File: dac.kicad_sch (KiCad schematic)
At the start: 30 parts, among them J2 Conn_02x03_Odd_Even, U6 PCM5242RHBR, X1 22.5792Mhz, X2 24.576Mhz

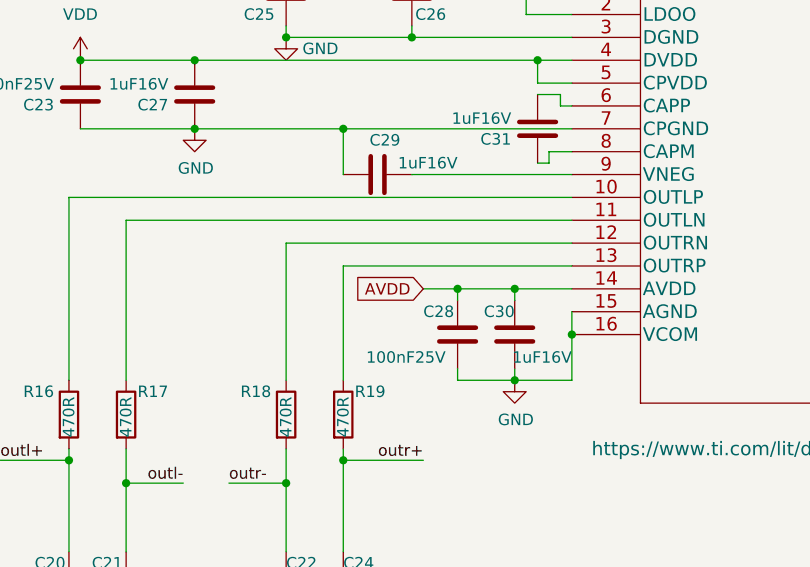
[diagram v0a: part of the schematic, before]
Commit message: Use Power Symbols for analog power
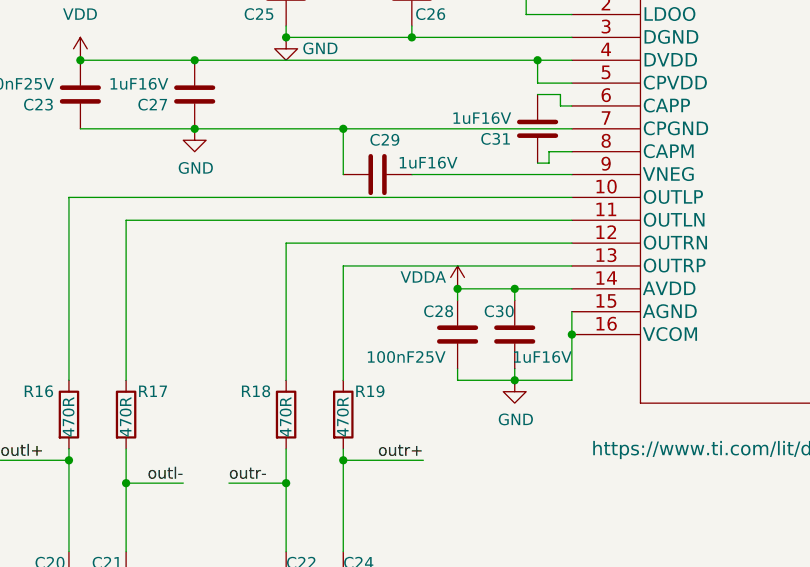
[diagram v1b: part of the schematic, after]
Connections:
- net AVDD renamed VDDA
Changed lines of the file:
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@@
     (comment 2 "License: CERN Open Hardware Licence Version 2 - Permissive")
   )
+  (junction (at 90.17 118.11) (diameter 0) (color 0 0 0 0)
+  )
   (junction (at 199.39 115.57) (diameter 0) (color 0 0 0 0)
   )
@@
   )
   (junction (at 154.94 87.63) (diameter 0) (color 0 0 0 0)
-  )
-  (junction (at 90.17 118.11) (diameter 0) (color 0 0 0 0)
   )
   (junction (at 71.12 90.17) (diameter 0) (color 0 0 0 0)
@@
   )
   (wire (pts (xy 71.12 90.17) (xy 85.09 90.17))
-    (stroke (width 0) (type default))
-  )
-  (wire (pts (xy 90.17 118.11) (xy 86.36 118.11))
     (stroke (width 0) (type default))
   )
@@
     (property "Intersheetrefs" "${INTERSHEET_REFS}" (at 179.1633 90.17 0)
       (effects (font (size 1.27 1.27)) (justify left) hide)
-    )
-  )
-  (global_label "AVDD" (shape input) (at 86.36 118.11 180)
-    (effects (font (size 1.27 1.27)) (justify right))
-    (property "Intersheetrefs" "${INTERSHEET_REFS}" (at 86.36 118.11 0)
-      (effects (font (size 1.27 1.27)) hide)
     )
   )
@@
         )
       )
+    )
+  )
+  (symbol (lib_id "power:VDDA") (at 90.17 118.11 0) (unit 1)
+    (in_bom yes) (on_board yes) (dnp no)
+    (property "Reference" "#PWR038" (at 90.17 121.92 0)
+      (effects (font (size 1.27 1.27)) hide)
+    )
+    (property "Value" "VDDA" (at 86.36 116.84 0)
+      (effects (font (size 1.27 1.27)))
+    )
+    (property "Footprint" "" (at 90.17 118.11 0)
+      (effects (font (size 1.27 1.27)) hide)
+    )
+    (property "Datasheet" "" (at 90.17 118.11 0)
+      (effects (font (size 1.27 1.27)) hide)
+    )
+    (pin "1")
+    (instances
+      (project "pedalboard-soundcard"
+        (path "/257597c6-fbef-4478-b0f4-968f2d6f1866/c0100554-f979-4e8d-b08c-e48cc1e12bdc"
+          (reference "#PWR038") (unit 1)
+        )
+      )

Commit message: Revert to standard RPI headers
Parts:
- J2: footprint Connector_PinHeader_2.54mm:PinHeader_2x03_P2.54mm_Vertical -> pedalboard-soundcard:PinSocket_2x03_P2.54mm_Vertical
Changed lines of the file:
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@@
       (effects (font (size 1.27 1.27)))
     )
-    (property "Footprint" "Connector_PinHeader_2.54mm:PinHeader_2x03_P2.54mm_Vertical" (at 130.81 158.75 0)
+    (property "Footprint" "pedalboard-soundcard:PinSocket_2x03_P2.54mm_Vertical" (at 130.81 158.75 0)
       (effects (font (size 1.27 1.27)) hide)
     )

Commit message: Fix library
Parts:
- U6: symbol zynthiandac-rescue:PCM5242RHBR-pcm5242 -> pedalboard-soundcard:PCM5242RHBR-pcm5242
- X1, X2: symbol zynthiandac-rescue:ASCO-Oscillator -> pedalboard-soundcard:ASCO-Oscillator
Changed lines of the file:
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@@
     )
   )
-  (symbol (lib_id "zynthiandac-rescue:ASCO-Oscillator") (at 214.63 115.57 0) (unit 1)
+  (symbol (lib_id "pedalboard-soundcard:ASCO-Oscillator") (at 214.63 115.57 0) (unit 1)
     (in_bom yes) (on_board yes) (dnp no)
     (property "Reference" "X2" (at 219.71 121.92 0)
@@
     )
   )
-  (symbol (lib_id "zynthiandac-rescue:PCM5242RHBR-pcm5242") (at 102.87 85.09 0) (unit 1)
+  (symbol (lib_id "pedalboard-soundcard:PCM5242RHBR-pcm5242") (at 102.87 85.09 0) (unit 1)
     (in_bom yes) (on_board yes) (dnp no)
     (property "Reference" "U6" (at 125.73 75.2602 0)
@@
     )
   )
-  (symbol (lib_id "zynthiandac-rescue:ASCO-Oscillator") (at 214.63 81.28 0) (unit 1)
+  (symbol (lib_id "pedalboard-soundcard:ASCO-Oscillator") (at 214.63 81.28 0) (unit 1)
     (in_bom yes) (on_board yes) (dnp no)
     (property "Reference" "X1" (at 219.71 87.63 0)
       (effects (font (size 1.27 1.27)) (justify left))
     )
-    (property "Value" "22.5792Mhz" (at 222.25 85.09 0)
-      (effects (font (size 1.27 1.27)) (justify left))
-    )
+    (property "Value" "22.5792Mhz" (at 223.52 85.09 0)
+      (effects (font (size 1.27 1.27)) (justify left))
+    )

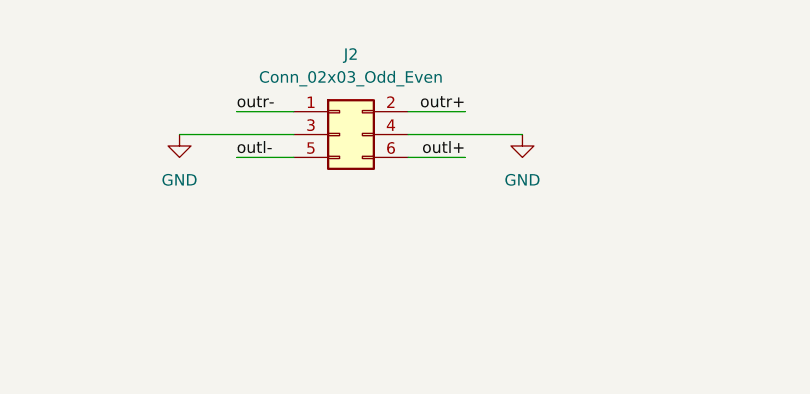
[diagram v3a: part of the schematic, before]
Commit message: Add 3.5mm jack connectors
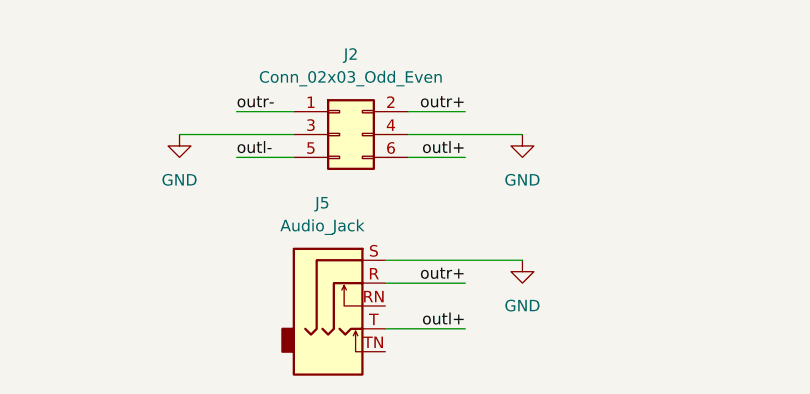
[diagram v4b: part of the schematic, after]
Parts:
- added J5: Audio_Jack, Connector_Audio:Jack_3.5mm_CUI_SJ1-3525N_Horizontal, symbol Connector_Audio:AudioJack3_SwitchTR
- J2: Supplier (none) -> https://www.digikey.ch/de/products/detail/te-connectivity-a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
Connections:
- net GND: now also J5.S
- net outl+: now also J5.T
- net outr+: now also J5.R
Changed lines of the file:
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@@
+    (stroke (width 0) (type default))
+  )
+  (wire (pts (xy 135.89 172.72) (xy 151.13 172.72))
     (stroke (width 0) (type default))
   )
@@
     (stroke (width 0) (type default))
   )
+  (wire (pts (xy 135.89 175.26) (xy 144.78 175.26))
+    (stroke (width 0) (type default))
+  )
   (wire (pts (xy 77.47 135.89) (xy 77.47 137.16))
     (stroke (width 0) (type default))
@@
     (stroke (width 0) (type default))
   )
+  (wire (pts (xy 135.89 180.34) (xy 144.78 180.34))
+    (stroke (width 0) (type default))
+  )
   (wire (pts (xy 238.76 85.09) (xy 238.76 88.9))
     (stroke (width 0) (type default))
@@
     (stroke (width 0) (type default))
   )
+  (label "outl+" (at 144.78 180.34 180) (fields_autoplaced)
+    (effects (font (size 1.27 1.27)) (justify right bottom))
+  )
   (label "outl-" (at 59.69 139.7 180) (fields_autoplaced)
+    (effects (font (size 1.27 1.27)) (justify right bottom))
+  )
+  (label "outr+" (at 144.78 175.26 180) (fields_autoplaced)
     (effects (font (size 1.27 1.27)) (justify right bottom))
   )
@@
     )
   )
+  (symbol (lib_id "Connector_Audio:AudioJack3_SwitchTR") (at 130.81 175.26 0) (unit 1)
+    (in_bom yes) (on_board yes) (dnp no) (fields_autoplaced)
+    (property "Reference" "J5" (at 128.905 166.37 0)
+      (effects (font (size 1.27 1.27)))
+    )
+    (property "Value" "Audio_Jack" (at 128.905 168.91 0)
+      (effects (font (size 1.27 1.27)))
+    )
+    (property "Footprint" "Connector_Audio:Jack_3.5mm_CUI_SJ1-3525N_Horizontal" (at 130.81 175.26 0)
+      (effects (font (size 1.27 1.27)) hide)
+    )
+    (property "Datasheet" "https://www.cuidevices.com/product/resource/sj1-352xng.pdf" (at 130.81 175.26 0)
+      (effects (font (size 1.27 1.27)) hide)
+    )
+    (property "Supplier" "https://www.digikey.ch/de/products/detail/schurter-inc/4833-2320/2644235" (at 130.81 175.26 0)
+      (effects (font (size 1.27 1.27)) hide)
+    )
+    (pin "RN")
+    (pin "S")
+    (pin "R")
+    (pin "TN")
+    (pin "T")
+    (instances
+      (project "pedalboard-soundcard"
+        (path "/257597c6-fbef-4478-b0f4-968f2d6f1866/c0100554-f979-4e8d-b08c-e48cc1e12bdc"
+          (reference "J5") (unit 1)
+        )
+      )
+    )
+  )
   (symbol (lib_id "power:GND") (at 199.39 91.44 0) (unit 1)
     (in_bom yes) (on_board yes) (dnp no)
@@
         (path "/684ba6b6-4674-4c20-b126-c7deb678f8f5"
           (reference "R27") (unit 1)
+        )
+      )
+    )
+  )
+  (symbol (lib_id "power:GND") (at 151.13 172.72 0) (unit 1)
+    (in_bom yes) (on_board yes) (dnp no) (fields_autoplaced)
+    (property "Reference" "#PWR041" (at 151.13 179.07 0)
+      (effects (font (size 1.27 1.27)) hide)
+    )
+    (property "Value" "GND" (at 151.13 177.8 0)
+      (effects (font (size 1.27 1.27)))
+    )
+    (property "Footprint" "" (at 151.13 172.72 0)
+      (effects (font (size 1.27 1.27)) hide)
+    )
+    (property "Datasheet" "" (at 151.13 172.72 0)
+      (effects (font (size 1.27 1.27)) hide)
+    )
+    (pin "1")
+    (instances
+      (project "pedalboard-soundcard"
+        (path "/257597c6-fbef-4478-b0f4-968f2d6f1866/c0100554-f979-4e8d-b08c-e48cc1e12bdc"
+          (reference "#PWR041") (unit 1)
         )
       )
@@
       (effects (font (size 1.27 1.27)) hide)
     )
-    (property "Datasheet" "~" (at 130.81 158.75 0)
-      (effects (font (size 1.27 1.27)) hide)
-    )
-    (property "Supplier" "" (at 130.81 158.75 0)
-      (effects (font (size 1.27 1.27)) hide)
-    )
+    (property "Datasheet" "https://www.te.com/commerce/DocumentDelivery/DDEController?Action=srchrtrv&DocNm=534206&DocType=Customer+Drawing&DocLang=English" (at 130.81 158.75 0)
+      (effects (font (size 1.27 1.27)) hide)
+    )
+    (property "Supplier" "https://www.digikey.ch/de/products/detail/te-connectivity-amp-connectors/5-534206-3/1093005" (at 130.81 158.75 0)
+      (effects (font (size 1.27 1.27)) hide)
+    )

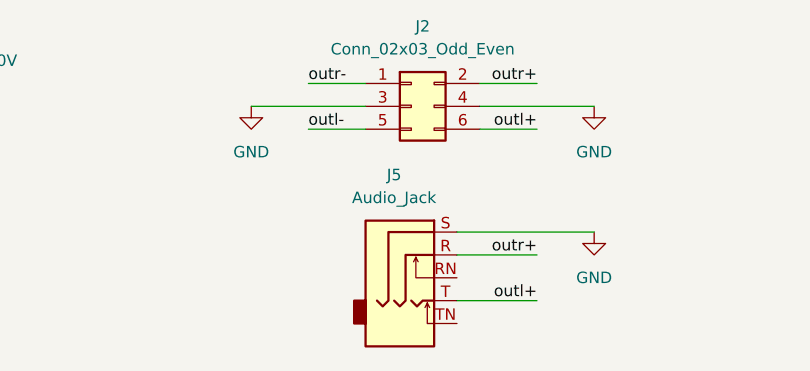
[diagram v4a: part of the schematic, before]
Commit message: DNP 3.5mm jack connectors
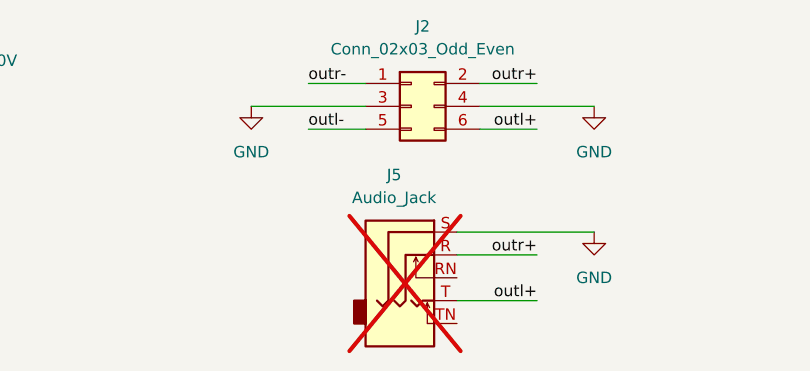
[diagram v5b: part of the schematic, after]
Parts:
- J5: now not fitted
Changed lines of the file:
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@@
   )
   (symbol (lib_id "Connector_Audio:AudioJack3_SwitchTR") (at 130.81 175.26 0) (unit 1)
-    (in_bom yes) (on_board yes) (dnp no) (fields_autoplaced)
+    (in_bom yes) (on_board yes) (dnp yes) (fields_autoplaced)
     (property "Reference" "J5" (at 128.905 166.37 0)
       (effects (font (size 1.27 1.27)))

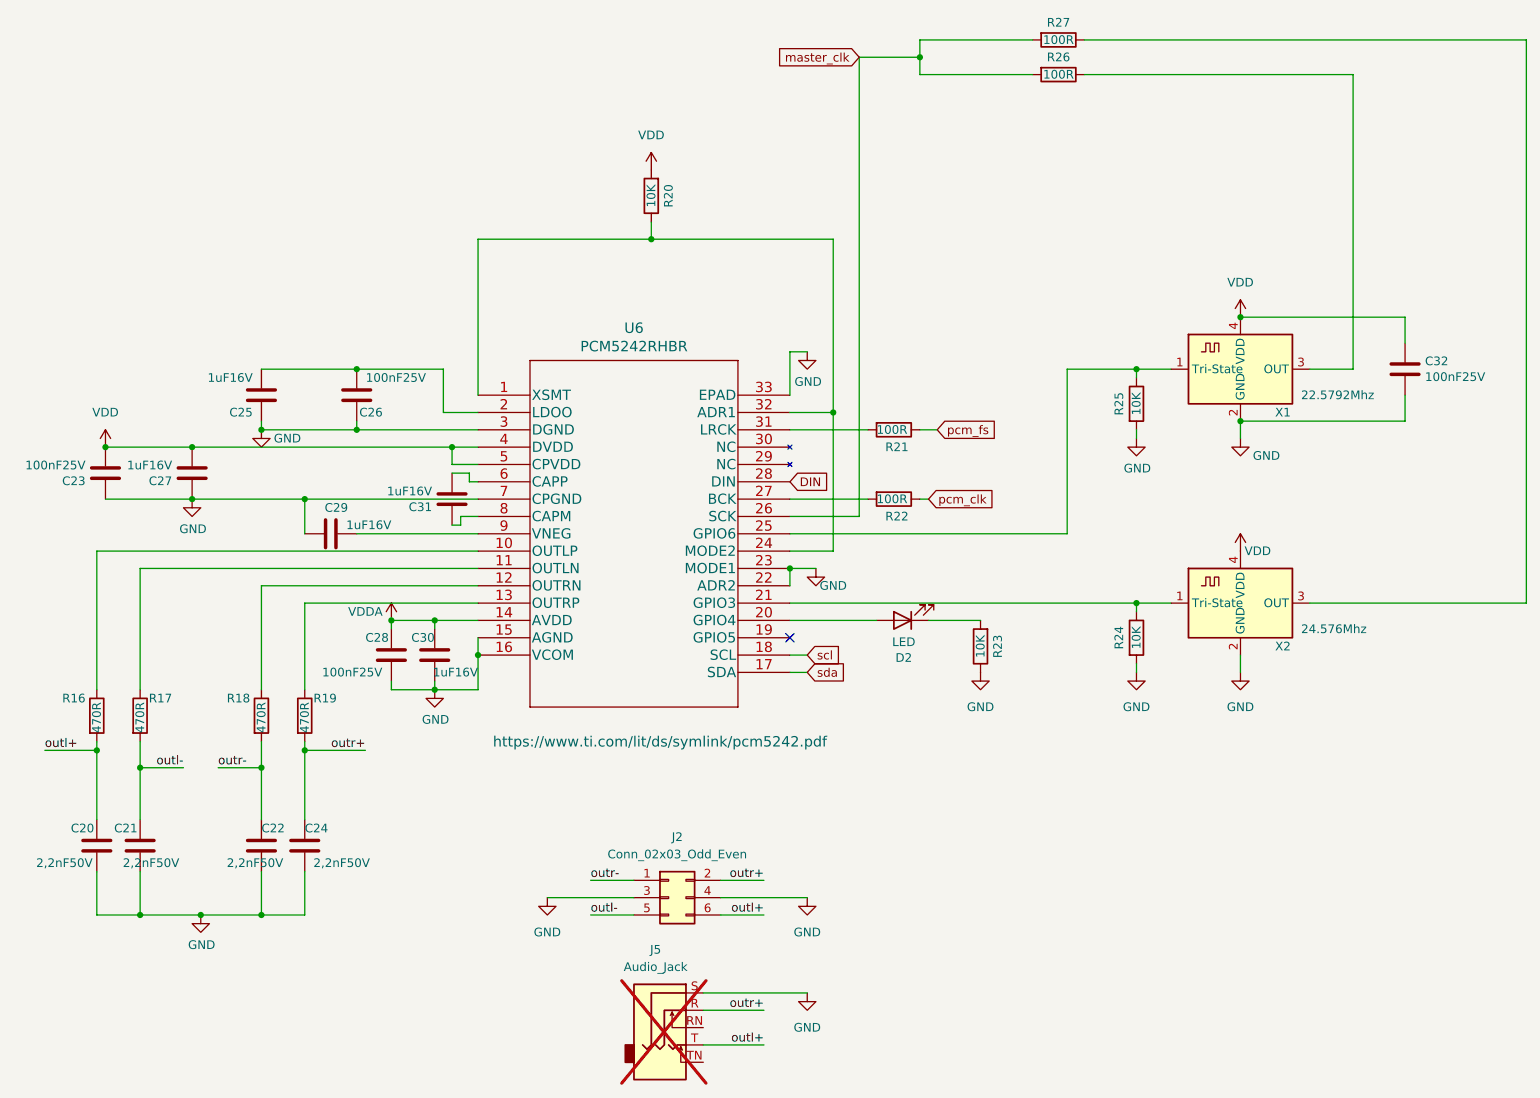
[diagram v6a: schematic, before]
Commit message: Add panel tabs
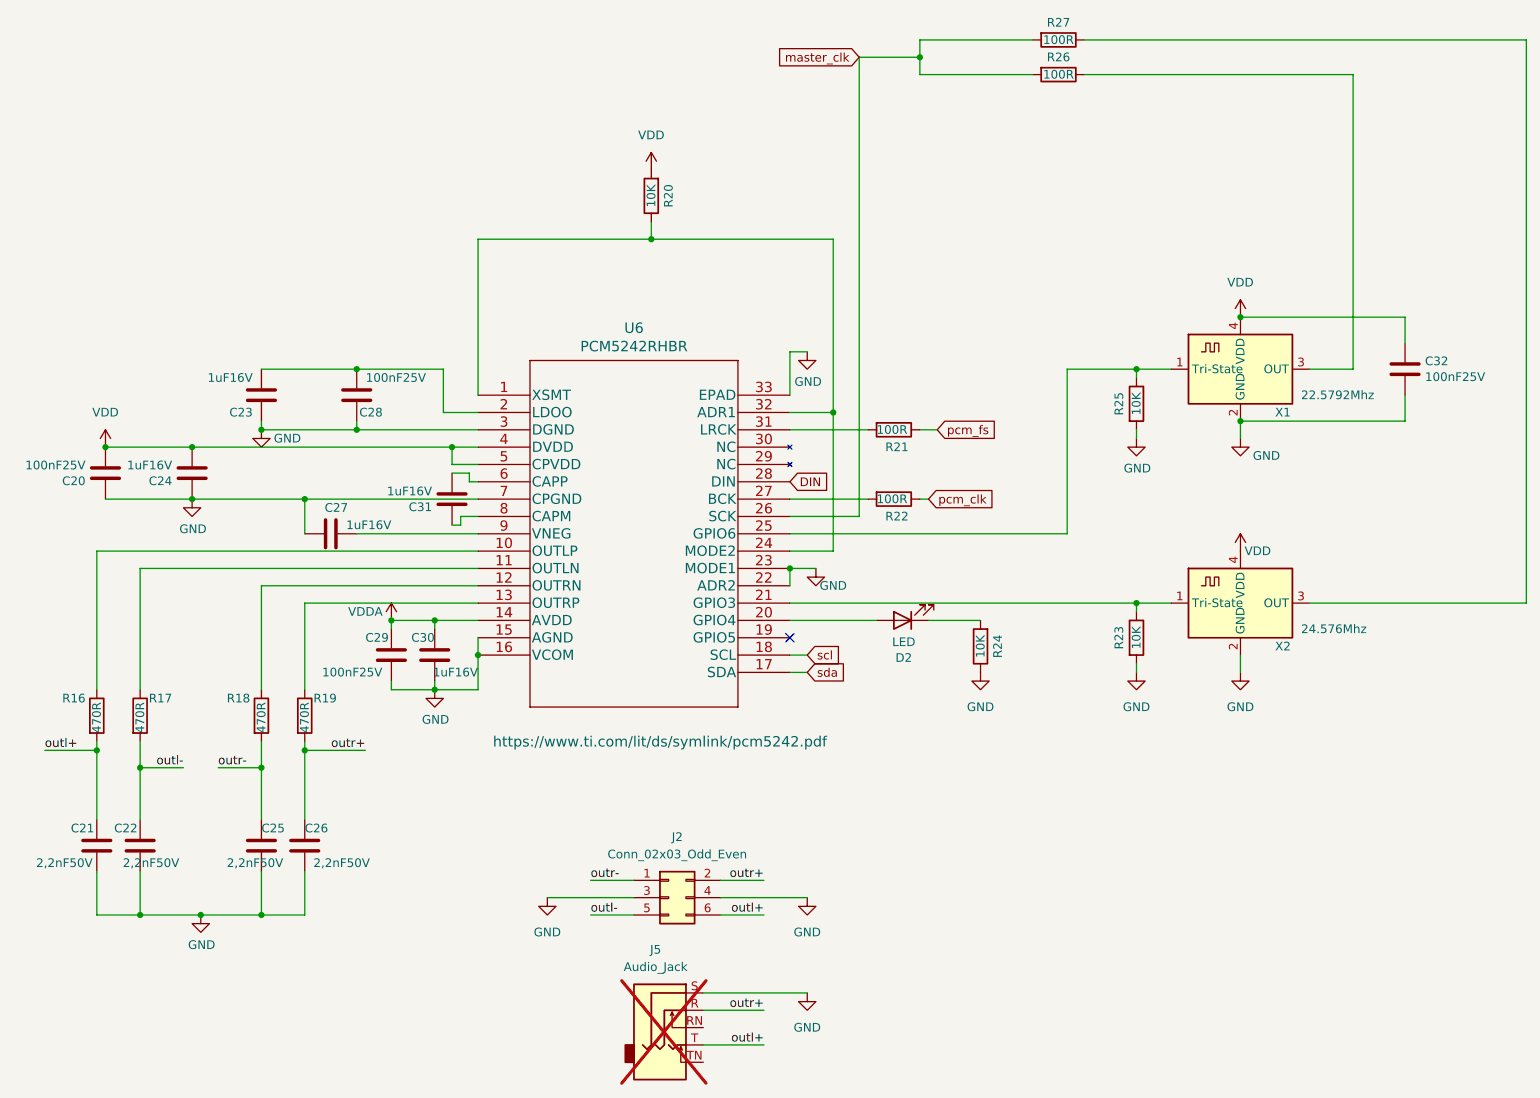
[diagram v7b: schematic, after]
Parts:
- renumbered C23 to C20, C20 to C21, C21 to C22, C25 to C23, C27 to C24, C22 to C25, C24 to C26, C29 to C27, C26 to C28, C28 to C29, R24 to R23, R23 to R24
